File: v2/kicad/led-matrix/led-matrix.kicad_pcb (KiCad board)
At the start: 2 copper layers, 38 x 38 mm, 6 parts, among them J1 Conn_02x03_Input, J2 Conn_02x03_Output, U1 MAX7219

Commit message: Routing attempt 3
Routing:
- net load: track 0.00 -> 57.6 mm
- net clk: track 0.00 -> 55.1 mm, vias 0 -> 1
- net D_fwd: track 0.00 -> 47.3 mm
- net column4: track 0.00 -> 29.2 mm, vias 0 -> 1
- net Dout: track 0.00 -> 27.7 mm
- net Vcc: track 5.51 -> 32.6 mm, vias 0 -> 1
- net row7: track 0.00 -> 26.7 mm, vias 0 -> 1
- net column2: track 0.00 -> 26.4 mm, vias 0 -> 1
- net row5: track 0.00 -> 26.0 mm, vias 0 -> 1
- net row2: track 0.00 -> 25.8 mm
- net row6: track 0.00 -> 23.1 mm, vias 0 -> 1
- net column1: track 0.00 -> 22.7 mm, vias 0 -> 1
- net row4: track 0.00 -> 21.2 mm, vias 0 -> 1
- net column7: track 0.00 -> 20.9 mm, vias 0 -> 1
- net column5: track 0.00 -> 20.1 mm
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- added copper zone on B.Cu, net GND
- added copper zone on F.Cu, net GND

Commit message: V2: Make PCB prettier
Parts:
- added REF**: MountingHole_2.2mm_M2_ISO7380, MountingHole:MountingHole_2.2mm_M2_ISO7380, F.Cu at (134.0, 104.0)
- added REF**: MountingHole_2.2mm_M2_ISO7380, MountingHole:MountingHole_2.2mm_M2_ISO7380, F.Cu at (104.0, 134.0)
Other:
- board text added: "CLK"
- board text added: "D_fwd"
- board text added: "D_in"
- board text added: "Dout"
- board text added: "GND"
- board text added: "Load"
- board text added: "Vcc"
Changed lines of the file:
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@@
       (effects (font (size 1 1) (thickness 0.15)))
     )
-    (fp_text value "Conn_02x03_Input" (at -5.65 7.85 90) (layer "F.Fab")
+    (fp_text value "Conn_02x03_Input" (at -5.65 7.85 90) (layer "F.Fab") hide
       (effects (font (size 1 1) (thickness 0.15)))
     )
@@
     (property "Sheetname" "")
     (attr smd)
-    (fp_text reference "C1" (at 0 -1.85) (layer "F.SilkS")
-      (effects (font (size 1 1) (thickness 0.15)))
-    )
-    (fp_text value "0.1 uF" (at 0 1.85) (layer "F.Fab")
-      (effects (font (size 1 1) (thickness 0.15)))
-    )
-    (fp_text user "${REFERENCE}" (at 0 0) (layer "F.Fab")
+    (fp_text reference "C1" (at 0 -1.85) (layer "F.SilkS") hide
+      (effects (font (size 1 1) (thickness 0.15)))
+    )
+    (fp_text value "0.1 uF" (at 0 1.85) (layer "F.SilkS")
+      (effects (font (size 1 1) (thickness 0.15)))
+    )
+    (fp_text user "${REFERENCE}" (at 0 0) (layer "F.SilkS")
       (effects (font (size 0.8 0.8) (thickness 0.12)))
     )
@@
     )
   )
+  (footprint "MountingHole:MountingHole_2.2mm_M2_ISO7380" (layer "F.Cu")
+    (at 134 104)
+    (descr "Mounting Hole 2.2mm, no annular, M2, ISO7380")
+    (tags "mounting hole 2.2mm no annular m2 iso7380")
+    (attr exclude_from_pos_files exclude_from_bom)
+    (fp_text reference "REF**" (at 0 -2.75) (layer "F.SilkS") hide
+      (effects (font (size 1 1) (thickness 0.15)))
+    )
+    (fp_text value "MountingHole_2.2mm_M2_ISO7380" (at 1.09 3.26) (layer "F.Fab") hide
+      (effects (font (size 1 1) (thickness 0.15)))
+    )
+    (fp_text user "${REFERENCE}" (at 0.3 0) (layer "F.Fab") hide
+      (effects (font (size 1 1) (thickness 0.15)))
+    )
+    (fp_circle (center 0 0) (end 1.75 0) (layer "Cmts.User") (width 0.15) (fill none))
+    (fp_circle (center 0 0) (end 2 0) (layer "F.CrtYd") (width 0.05) (fill none))
+    (pad "" np_thru_hole circle (at 0 0) (size 2.2 2.2) (drill 2.2) (layers *.Cu *.Mask))
+  )
+  (footprint "MountingHole:MountingHole_2.2mm_M2_ISO7380" (layer "F.Cu")
+    (at 104 134)
+    (descr "Mounting Hole 2.2mm, no annular, M2, ISO7380")
+    (tags "mounting hole 2.2mm no annular m2 iso7380")
+    (attr exclude_from_pos_files exclude_from_bom)
+    (fp_text reference "REF**" (at 0 -2.75) (layer "F.SilkS") hide
+      (effects (font (size 1 1) (thickness 0.15)))
+    )
+    (fp_text value "MountingHole_2.2mm_M2_ISO7380" (at 0 2.75) (layer "F.Fab") hide
+      (effects (font (size 1 1) (thickness 0.15)))
+    )
+    (fp_text user "${REFERENCE}" (at 0.3 0) (layer "F.Fab") hide
+      (effects (font (size 1 1) (thickness 0.15)))
+    )
+    (fp_circle (center 0 0) (end 1.75 0) (layer "Cmts.User") (width 0.15) (fill none))
+    (fp_circle (center 0 0) (end 2 0) (layer "F.CrtYd") (width 0.05) (fill none))
+    (pad "" np_thru_hole circle (at 0 0) (size 2.2 2.2) (drill 2.2) (layers *.Cu *.Mask))
+  )
   (footprint "Resistor_SMD:R_1206_3216Metric_Pad1.30x1.75mm_HandSolder" (layer "F.Cu")
     (at 114.55 129 180)
@@
     (property "Sheetname" "")
     (attr smd)
-    (fp_text reference "R1" (at 0 -1.82) (layer "F.SilkS")
-      (effects (font (size 1 1) (thickness 0.15)))
-    )
-    (fp_text value "28 K" (at 0 1.82) (layer "F.Fab")
-      (effects (font (size 1 1) (thickness 0.15)))
-    )
-    (fp_text user "${REFERENCE}" (at 0 0) (layer "F.Fab")
+    (fp_text reference "R1" (at 0 -1.82) (layer "F.SilkS") hide
+      (effects (font (size 1 1) (thickness 0.15)))
+    )
+    (fp_text value "28 K" (at 0 1.82) (layer "F.SilkS")
+      (effects (font (size 1 1) (thickness 0.15)))
+    )
+    (fp_text user "${REFERENCE}" (at 0 0) (layer "F.SilkS")
       (effects (font (size 0.8 0.8) (thickness 0.12)))
     )
@@
       (effects (font (size 1 1) (thickness 0.15)))
     )
-    (fp_text value "Conn_02x03_Output" (at 5.655 7.35 90) (layer "F.Fab")
+    (fp_text value "Conn_02x03_Output" (at 5.655 7.35 90) (layer "F.Fab") hide
       (effects (font (size 1 1) (thickness 0.15)))
     )
@@
     (property "Sheetname" "")
     (attr smd)
-    (fp_text reference "U1" (at 0 -8.65 90) (layer "F.SilkS")
-      (effects (font (size 1 1) (thickness 0.15)))
-    )
-    (fp_text value "MAX7219" (at 0 8.65 90) (layer "F.Fab")
-      (effects (font (size 1 1) (thickness 0.15)))
-    )
-    (fp_text user "${REFERENCE}" (at 0 0 90) (layer "F.Fab")
+    (fp_text reference "U1" (at 0 -8.65 90) (layer "F.SilkS") hide
+      (effects (font (size 1 1) (thickness 0.15)))
+    )
+    (fp_text value "MAX7219" (at 0 8.65 90) (layer "F.SilkS")
+      (effects (font (size 1 1) (thickness 0.15)))
+    )
+    (fp_text user "${REFERENCE}" (at 0 0 90) (layer "F.SilkS")
       (effects (font (size 1 1) (thickness 0.15)))
     )
@@
   )
   (gr_rect (start 100 100) (end 138 138) (layer "Edge.Cuts") (width 0.1) (fill none))
+  (gr_text "GND" (at 129.31 134.18) (layer "F.SilkS")
+    (effects (font (size 1 1) (thickness 0.15)))
+  )
+  (gr_text "D_fwd" (at 110.96 103.57) (layer "F.SilkS")
+    (effects (font (size 1 1) (thickness 0.15)))
+  )
+  (gr_text "Dout" (at 132.69 134.08) (layer "F.SilkS")
+    (effects (font (size 1 1) (thickness 0.15)))
+  )
+  (gr_text "D_in" (at 110.42 102.01) (layer "F.SilkS")
+    (effects (font (size 1 1) (thickness 0.15)))
+  )
+  (gr_text "Load" (at 102.56 102) (layer "F.SilkS")
+    (effects (font (size 1 1) (thickness 0.15)))
+  )
+  (gr_text "CLK" (at 129.21 132.63) (layer "F.SilkS")
+    (effects (font (size 1 1) (thickness 0.15)))
+  )
+  (gr_text "GND" (at 106.41 102.01) (layer "F.SilkS")
+    (effects (font (size 1 1) (thickness 0.15)))
+  )
+  (gr_text "CLK" (at 106.29 103.62) (layer "F.SilkS")
+    (effects (font (size 1 1) (thickness 0.15)))
+  )
+  (gr_text "Vcc" (at 102.23 103.6) (layer "F.SilkS")
+    (effects (font (size 1 1) (thickness 0.15)))
+  )
+  (gr_text "Vcc" (at 125.22 134.07) (layer "F.SilkS")
+    (effects (font (size 1 1) (thickness 0.15)))
+  )
+  (gr_text "Load" (at 125.55 132.6) (layer "F.SilkS")
+    (effects (font (size 1 1) (thickness 0.15)))
+  )
+  (gr_text "D_fwd" (at 133.13 132.61) (layer "F.SilkS")
+    (effects (font (size 1 1) (thickness 0.15)))
+  )
   (via (at 127.25 132) (size 0.8) (drill 0.4) (layers "F.Cu" "B.Cu") (free) (net 1))
   (segment (start 117.635 124.65) (end 117.635 127.465) (width 0.5) (layer "F.Cu") (net 2))

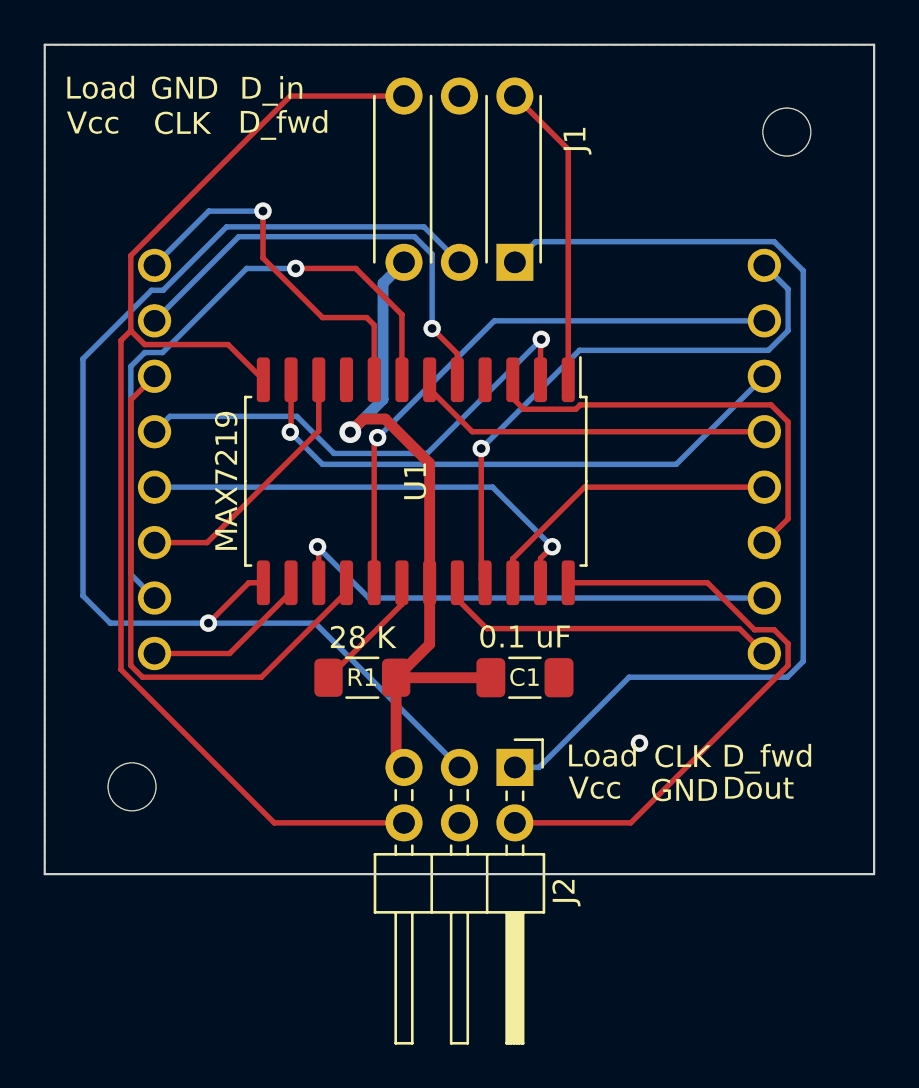
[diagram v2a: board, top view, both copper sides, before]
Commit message: Changed footprint to handsoldering and added logo
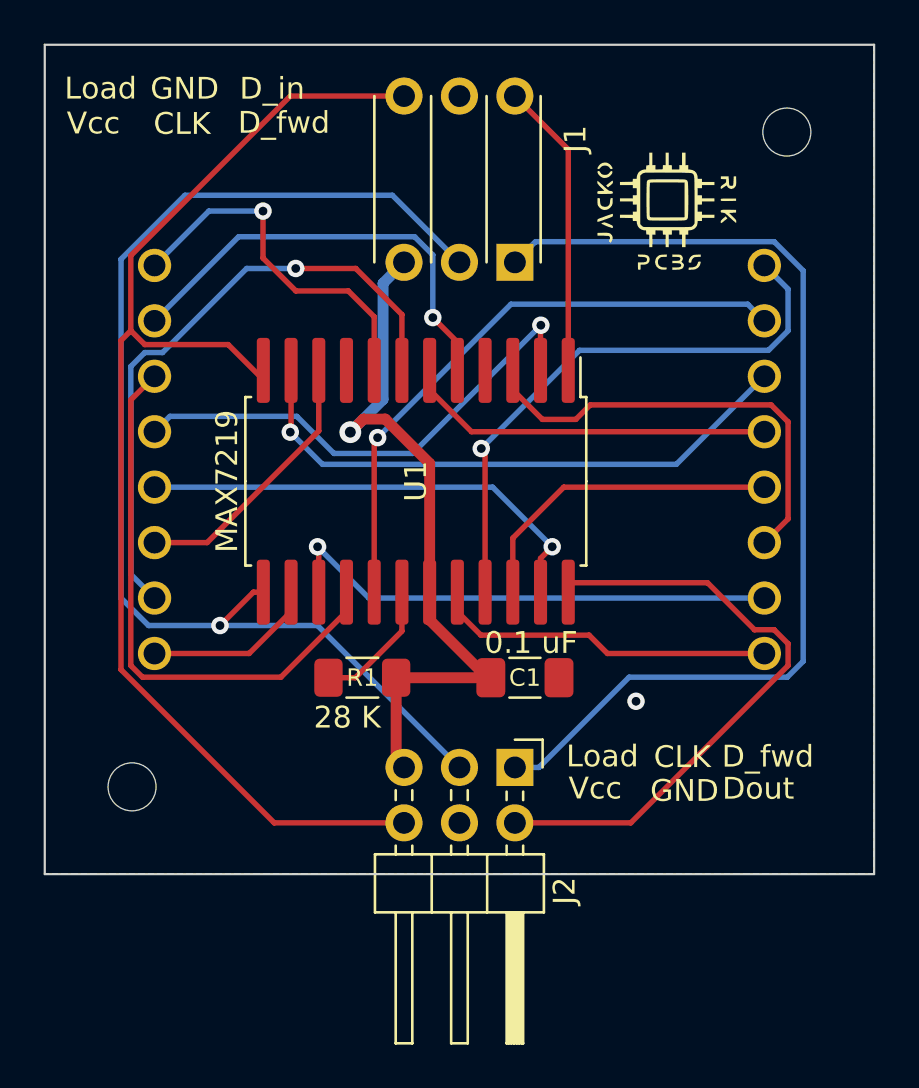
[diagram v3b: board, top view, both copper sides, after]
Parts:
- added G***: LOGO, led-matrix:logo_scaled, F.Cu at (128.5, 107.6)
- U1: footprint Package_SO:SOIC-24W_7.5x15.4mm_P1.27mm -> led-matrix:HandSolder.SOIC-24W_7.5x15.4mm_P1.27mm
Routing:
- net row8: track 14.0 -> 15.0 mm
- net column3: track 16.6 -> 17.4 mm
- net row7: track 26.7 -> 27.3 mm
- net column5: track 20.1 -> 20.6 mm

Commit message: Aesthetics updates to PCB
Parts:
- moved G*** 12.8 mm to (128.4, 120.4)
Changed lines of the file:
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@@
   (paper "A4")
   (title_block
-    (title "Ir.")
-    (date "Vandaag")
-    (rev ">0")
-    (company "Ja, leuk")
+    (title "LED MATRIX 2.0")
+    (date "2022-02-04")
+    (rev "1.0")
+    (company "Jacko & Rik PCBs inc.")
   )
   (layers
@@
     (property "Sheetname" "")
     (attr through_hole)
-    (fp_text reference "J1" (at -5.65 -2.77 -90) (layer "F.SilkS")
+    (fp_text reference "J1" (at -5.65 -2.77 -90) (layer "F.SilkS") hide
       (effects (font (size 1 1) (thickness 0.15)))
     )
@@
   )
   (footprint "led-matrix:logo_scaled" (layer "F.Cu")
-    (at 128.482113 107.627757)
+    (at 128.4 120.43)
     (attr board_only exclude_from_pos_files exclude_from_bom)
     (fp_text reference "G***" (at 0 0) (layer "F.SilkS") hide
@@
     (property "Sheetname" "")
     (attr through_hole)
-    (fp_text reference "D1" (at 0 7 unlocked) (layer "B.SilkS")
+    (fp_text reference "D1" (at 0 7 unlocked) (layer "B.SilkS") hide
       (effects (font (size 1 1) (thickness 0.15)) (justify mirror))
     )
